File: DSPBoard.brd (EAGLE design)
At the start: 416 x 128.5 mm, 449 parts, among them IC1 AD1939WBSTZ, IC10 LM833D, IC11 LM833D, IC12 TL074D, IC2 24AA1025, IC29 TL074D, IC3 LM4040B10DBZ, IC4 LM833D, IC5 LM833D, IC6 LM833D, IC7 LM833D, IC8 LM833D, IC9 LM833D, U1 LM11173.3NOPB, U2 PEC11R-4315F-N0012, U3 PEC11R-4315F-N0012, X1 2510-, Y1 12.288MHz

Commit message: double-check and confirm opamp audio gains (not CV)
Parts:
- removed C133, C49, C58, C69: 10nF, rcl:C0603
- added C160: 10uF, rcl:C0603
- added C161: 0.1uF, rcl:C0603
- added CBST: 100nF, AcceleratedDesigns_Lib:0603
- added CIN: 22uF, AcceleratedDesigns_Lib:0805
- added COUT: 47uF, AcceleratedDesigns_Lib:1206
- added GND: WB_GND, AcceleratedDesigns_Lib:WB_GND
- added IOUT: WB_CURRENT_LOAD, AcceleratedDesigns_Lib:WB_CURRENT_LOAD
- added JP17, JP18, JP19, JP20: JUMPER-SMT_2_NC_PASTE_SILK, SparkFun-Jumpers:SMT-JUMPER_2_NC_PASTE_SILK
- added L1: 4.7uH, AcceleratedDesigns_Lib:CDPH4D19F
- added R182, R183, R184, R185: 100, rcl:R0603
- added RFBB: 10k, AcceleratedDesigns_Lib:0201
- added RFBT: 61.9k, AcceleratedDesigns_Lib:0402
- added SV2: (no value), con-lstb:MA04-1
- added U4: TPS561201DDCR, AcceleratedDesigns_Lib:DDC0006A
- added VIN: WB_BATTERY, AcceleratedDesigns_Lib:WB_BATTERY
- C119, C121: value 22uF -> 47uF; device rcl:C0603 -> rcl:PANASONIC_D
- C122: value 0.1u -> 390pF
- C123: value 0.1u -> 5.6nF
- C137: value 0.1uF -> 100uF
- C32: value 0.1uF -> 10uF
- R135: value 562 -> 562R
- R15, R31, R49, R65: value 15k -> 18k
- R364, R368, R369, R370: value 33R -> 2k2
- R39, R46, R62, R72: value 10k -> 6k2
- moved IC3 23.6 mm to (95.3, 32.7)
- moved C45 23.6 mm to (93.8, 34.0)
- moved J1 23.6 mm to (91.6, 31.4)
- moved R16 23.6 mm to (96.0, 31.4)
- moved R5 22.7 mm to (106.0, 14.5)
- moved R4 20.6 mm to (106.4, 12.6), turned to 180 degrees
- moved C29 19.9 mm to (108.6, 13.6), turned to 90 degrees
- moved U$11 17.6 mm to (112.4, 6.37), turned to 180 degrees
- moved C30 12.7 mm to (113.1, 17.5), turned to 270 degrees
- moved U$3 12.5 mm to (115.6, 17.0), flipped to the top, turned to 90 degrees
- moved C31 8.60 mm to (115.5, 14.0)
- moved SV1 7.73 mm to (123.6, 12.3), turned to 270 degrees
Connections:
- removed net DSDATA3: IC1.18
- removed net DSDATA4: IC1.15
- removed net N$234: D1.3, D3.3, D5.3, D7.3
- removed net N$235: D2.3, D4.3, D6.3, D8.3
- removed net N$549: IC2.6, R364.2
- removed net N$552: IC2.5, R368.2
- removed net N$553: R370.1, U$1.31
- removed net N$554: R369.1, U$1.30
- new net 0: CIN.2, COUT.2, GND.1, IOUT.2, RFBB.2, U4.1, VIN.2
- new net 1: CIN.1, U4.3, U4.5, VIN.1
- new net 2: CBST.1, L1.1, U4.2
- new net 3: RFBB.1, RFBT.2, U4.4
- new net 4: COUT.1, IOUT.1, L1.2, RFBT.1
- new net 5: CBST.2, U4.6
- new net N$135: IC1.35, JP20.1, SV2.1
- new net N$158: IC1.34, JP19.1, SV2.2
- new net N$159: IC1.31, JP18.1, SV2.3
- new net N$160: R182.2, R39.1
- new net N$161: R185.2, R46.1
- new net N$162: R183.2, R62.1
- new net N$163: R184.2, R72.1
- new net N$7: IC1.30, JP17.1, SV2.4
- net +3V3: now also C160.2, C161.2, R364.2, R368.1, R369.1, R370.1
- net AIN0+: now also D2.3
- net AIN0-: now also D1.3
- net AIN1+: now also D4.3
- net AIN1-: now also D3.3
- net AIN2+: now also D7.3
- net AIN2-: now also D8.3
- net AIN3+: now also D6.3
- net AIN3-: now also D5.3
- net ASDATA2: no longer IC1.26
- net DSDATA2: no longer IC1.19
- net FILTR: now also C121.+; no longer C121.1
- net GND: now also C119.-, C121.-, C160.1, C161.1, JP17.2, JP18.2, JP19.2, JP20.2; no longer C119.2, C121.2, IC1.30, IC1.31, IC1.34, IC1.35
- net MP2: now also IC2.6
- net MP3: now also IC2.5, R368.2; no longer R368.1
- net N$10: no longer C49.1
- net N$18: now also R182.1; no longer R39.1
- net N$36: now also R185.1; no longer R46.1
- net N$38: no longer C58.2
- net N$40: no longer C58.1
- net N$47: now also R183.1; no longer R62.1
- net N$48: no longer C69.2
- net N$49: no longer C69.1
- net N$56: now also R184.1; no longer R72.1
- net N$57: no longer C133.2
- net N$58: no longer C133.1
- net N$75: now also C119.+; no longer C119.1
- net N$9: no longer C49.2
- net S_SCL: now also U$1.31
- net S_SDA: now also U$1.30
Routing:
- net GND: track 153.9 -> 103.5 mm, vias 13 -> 16
- net +12V: track 50.8 -> 20.3 mm, vias 2 -> 1
- net +5V: track 41.3 -> 13.1 mm, vias 3 -> 1
- net N$8: track 4.24 -> 19.3 mm, vias 1 -> 0
- net -12V: track 5.11 -> 0.00 mm
- net N$5: track 13.7 -> 9.35 mm, vias 1 -> 2
- net N$2: track 4.12 -> 0.00 mm, vias 1 -> 0
- net N$554: track 2.60 -> 0.00 mm
- net N$553: track 2.57 -> 0.00 mm
- net DSDATA2: track 2.38 -> 0.01 mm
- added copper zone on layer 1, net +12V
- added copper zone on layer 1, net +5V
- added copper zone on layer 1, net GND
- added copper zone on layer 16, net GND
- added copper zone on layer 1, net N$2
- added copper zone on layer 1, net N$5
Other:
- outline, holes or cut-outs redrawn
- board text removed: "Power Supplies"

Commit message: Chekcing and some bug fixes complete, plus psu layout touchup
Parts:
- removed C156: 100n, rcl:C0603
- removed CBST: 100nF, AcceleratedDesigns_Lib:0603
- removed CIN: 22uF, AcceleratedDesigns_Lib:0805
- removed COUT: 47uF, AcceleratedDesigns_Lib:1206
- removed GND: WB_GND, AcceleratedDesigns_Lib:WB_GND
- removed IOUT: WB_CURRENT_LOAD, AcceleratedDesigns_Lib:WB_CURRENT_LOAD
- removed L1: 4.7uH, AcceleratedDesigns_Lib:CDPH4D19F
- removed MUX1_RIPPLECOUNTER, MUX2_RIPPLECOUNTER: 4024D, 40xx:SO14
- removed RFBB: 10k, AcceleratedDesigns_Lib:0201
- removed RFBT: 61.9k, AcceleratedDesigns_Lib:0402
- removed U4: TPS561201DDCR, AcceleratedDesigns_Lib:DDC0006A
- removed VIN: WB_BATTERY, AcceleratedDesigns_Lib:WB_BATTERY
- added IC13: 4520D, 45xx:SO16
- C128, C129, C130, C131, C146, C147, C150, C151: value 0.1u -> 1n
- moved U$29 242.3 mm to (234.9, -81.2)
- moved U$5 208.0 mm to (9.66, 120.7), turned to 0 degrees
- moved U$6 200.7 mm to (22.1, 120.7), turned to 0 degrees
- moved U$7 194.7 mm to (34.6, 120.7), turned to 0 degrees
- moved U$21 189.9 mm to (47.0, 120.7), turned to 0 degrees
- moved IC11 183.0 mm to (101.6, 103.2), turned to 180 degrees
- moved IC10 163.0 mm to (91.5, 103.2), turned to 180 degrees
- moved C124 156.0 mm to (9.73, -47.5), turned to 90 degrees
- moved R2 155.6 mm to (8.17, 89.8), turned to 0 degrees
- moved U$8 155.1 mm to (59.4, 120.7)
- moved C26 153.9 mm to (9.78, 79.1)
- moved U$10 152.8 mm to (7.03, 84.9), turned to 90 degrees
- moved C125 152.5 mm to (5.13, -44.0), turned to 90 degrees
- moved R3 151.2 mm to (11.2, 89.8), turned to 0 degrees
- moved R10 150.6 mm to (0.54, -40.3), turned to 0 degrees
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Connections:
- removed net 0: CIN.2, COUT.2, GND.1, IOUT.2, RFBB.2, U4.1, VIN.2
- removed net 1: CIN.1, U4.3, U4.5, VIN.1
- removed net 2: CBST.1, L1.1, U4.2
- removed net 3: RFBB.1, RFBT.2, U4.4
- removed net 4: COUT.1, IOUT.1, L1.2, RFBT.1
- removed net 5: CBST.2, U4.6
- net +5V: now also IC13.16; no longer C156.1, MUX1_RIPPLECOUNTER.14, MUX2_RIPPLECOUNTER.14
- net GND: now also IC12.12, IC12.5, IC13.8, IC29.12, IC29.5; no longer C156.2, IC12.13, IC12.6, IC29.13, IC29.6, MUX1_RIPPLECOUNTER.7, MUX2_RIPPLECOUNTER.7
- net MUX1_A: now also IC13.3; no longer MUX1_RIPPLECOUNTER.12
- net MUX1_B: now also IC13.4; no longer MUX1_RIPPLECOUNTER.11
- net MUX1_C: now also IC13.5; no longer MUX1_RIPPLECOUNTER.9
- net MUX2_A_A: now also IC13.11; no longer MUX2_RIPPLECOUNTER.12
- net MUX2_A_B: now also IC13.12; no longer MUX2_RIPPLECOUNTER.11
- net MUX2_A_C: now also IC13.13; no longer MUX2_RIPPLECOUNTER.9
- net N$116: now also IC12.6; no longer IC12.5
- net N$122: now also IC12.13; no longer IC12.12
- net N$540: now also IC29.6; no longer IC29.5
- net N$543: now also IC29.13; no longer IC29.12
- net SDATA_OUT2_LRCLK: now also IC13.1, IC13.9; no longer MUX1_RIPPLECOUNTER.1, MUX2_RIPPLECOUNTER.1
- net SEL1: now also IC13.10, IC13.2; no longer MUX1_RIPPLECOUNTER.2
- net SEL2: now also IC13.15, IC13.7; no longer MUX2_RIPPLECOUNTER.2
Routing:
- net +3V3: track 117.9 -> 17.0 mm, vias 10 -> 2
- net GND: track 103.5 -> 35.3 mm, vias 16 -> 9
- net N$212: track 52.7 -> 10.8 mm, vias 5 -> 0
- net N$31: track 38.6 -> 1.72 mm
- net N$32: track 45.6 -> 8.72 mm
- net 3V3A: track 18.7 -> 0.00 mm, vias 2 -> 0
- net N$6: track 4.16 -> 21.8 mm, vias 1 -> 0
- net +5V: track 13.1 -> 8.03 mm, vias 1 -> 0
- net N$27: track 3.34 -> 0.00 mm
- net N$28: track 3.94 -> 0.70 mm
- net S_AUX_ADC2: track 3.18 -> 0.00 mm
- net N$141: track 3.18 -> 0.00 mm
- net N$120: track 3.13 -> 0.00 mm
- net S_AUX_ADC1: track 3.02 -> 0.00 mm
- net RESET: track 2.90 -> 0.00 mm
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- added copper zone on layer 1, net 3V3A
- added copper zone on layer 1, net N$3
- added copper zone on layer 1, net N$4

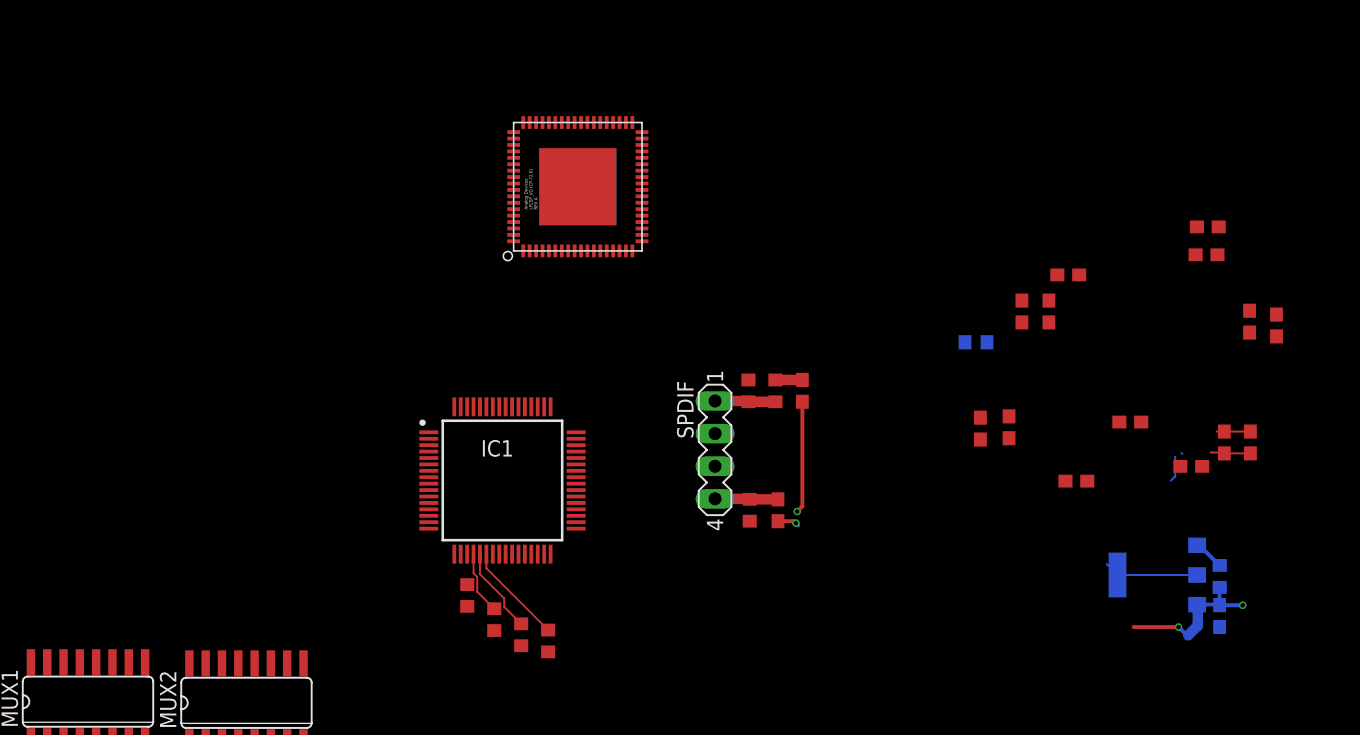
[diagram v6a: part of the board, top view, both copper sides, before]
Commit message: routing for the DSP
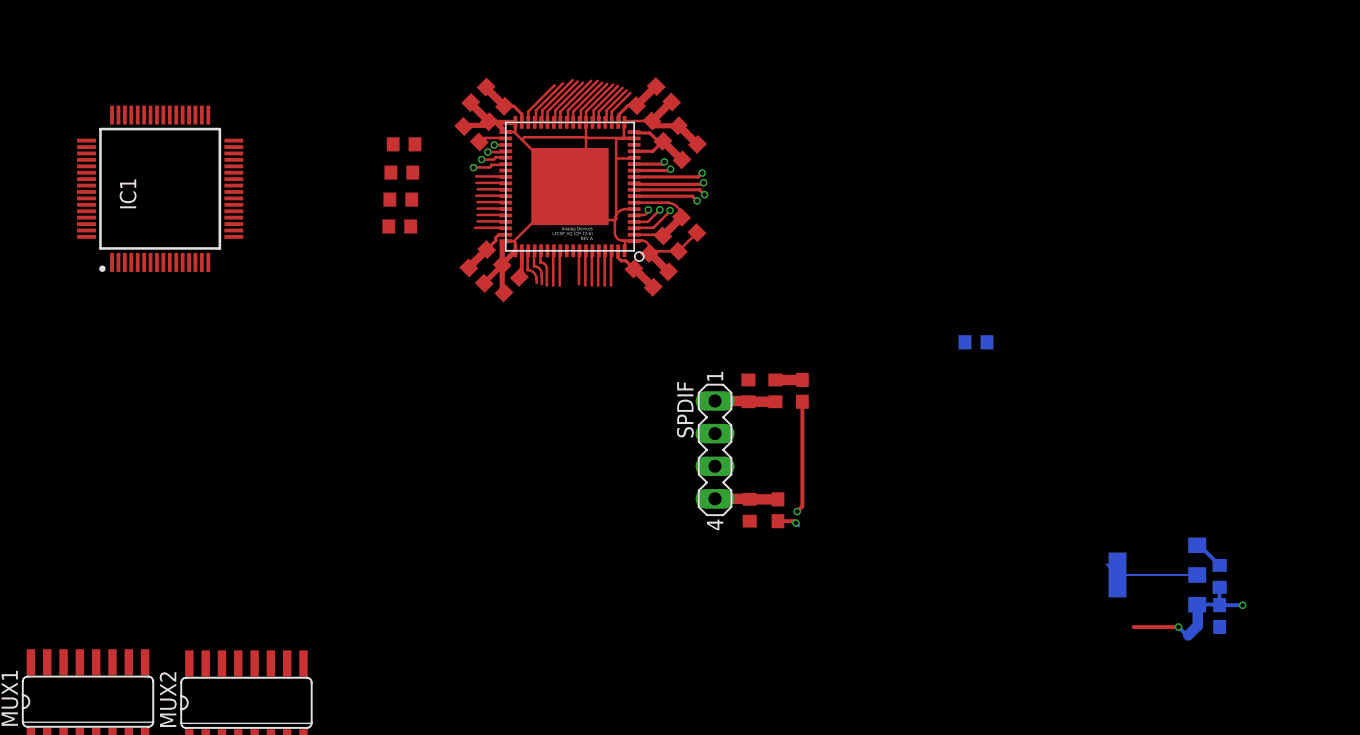
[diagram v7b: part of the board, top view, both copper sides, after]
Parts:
- moved C22 62.3 mm to (93.2, 83.9), turned to 135 degrees
- moved C15 60.6 mm to (95.0, 74.3), turned to 315 degrees
- moved C14 59.7 mm to (93.6, 72.9), turned to 315 degrees
- moved C16 47.7 mm to (110.2, 82.5), turned to 45 degrees
- moved C8 47.0 mm to (93.8, 87.0), turned to 225 degrees
- moved C7 46.8 mm to (95.2, 85.5), turned to 225 degrees
- moved C19 46.6 mm to (96.4, 72.1), turned to 225 degrees
- moved C13 44.0 mm to (106.5, 74.0), turned to 45 degrees
- moved C18 43.4 mm to (110.2, 76.8), turned to 315 degrees
- moved C11 42.8 mm to (108.0, 72.6), turned to 45 degrees
- moved R18 40.3 mm to (88.0, 83.1), turned to 0 degrees
- moved C21 38.4 mm to (108.7, 75.4), turned to 315 degrees
- moved R19 37.2 mm to (87.8, 80.9), turned to 0 degrees
- moved C9 35.1 mm to (106.7, 85.5), turned to 315 degrees
- moved IC1 35.0 mm to (69.0, 79.6), turned to 90 degrees
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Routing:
- net GND: track 35.3 -> 120.6 mm
- net +3V3: track 17.0 -> 36.3 mm
- net N$212: track 10.8 -> 24.5 mm
- net DLRCLK: track 7.90 -> 0.00 mm
- net DBCLK: track 6.76 -> 0.00 mm
- net S_AUX_ADC1: track 0.00 -> 5.64 mm, vias 0 -> 1
- net S_AUX_ADC2: track 0.00 -> 5.49 mm, vias 0 -> 1
- net S_AUX_ADC3: track 0.00 -> 5.43 mm, vias 0 -> 1
- net S_AUX_ADC0: track 0.00 -> 5.05 mm, vias 0 -> 1
- net DSDATA1: track 4.92 -> 0.01 mm
- net N$157: track 0.00 -> 4.30 mm
- net MP2: track 0.00 -> 4.23 mm
- net MP3: track 0.00 -> 4.23 mm
- net S_SCL: track 0.00 -> 4.16 mm
- net MP1: track 0.00 -> 4.02 mm
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
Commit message: grinding through
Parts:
- moved IC13 691.6 mm to (355.1, 142.4)
- moved JP10 582.5 mm to (368.5, 31.3)
- moved JP9 563.6 mm to (359.2, 16.6), turned to 270 degrees
- moved C160 562.1 mm to (218.3, 148.0)
- moved C161 562.1 mm to (218.3, 143.1)
- moved JP14 562.1 mm to (249.4, 174.7)
- moved JP15 562.1 mm to (240.8, 174.7)
- moved JP16 562.1 mm to (232.2, 174.7)
- moved R182 533.5 mm to (196.4, 118.1)
- moved R184 527.4 mm to (176.2, 133.1)
- moved C159 520.5 mm to (218.8, 83.7), flipped to the bottom, turned to 90 degrees
- moved JP2 519.0 mm to (390.5, 16.3)
- moved R183 516.1 mm to (167.2, 131.0)
- moved JP20 492.8 mm to (182.5, 75.3)
- moved JP19 489.0 mm to (180.0, 75.3)
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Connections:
- net ASDATA2: now also IC1.26
- net DSDATA2: now also IC1.19
- net ENCODER0_0: now also JP4.2; no longer JP4.1
- net S_AUX_ADC1: now also JP4.1; no longer JP4.2
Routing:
- net RESET: track 3.67 -> 108.1 mm, vias 0 -> 2
- net GND: track 120.6 -> 216.7 mm, vias 9 -> 10
- net +3V3: track 36.3 -> 124.0 mm, vias 2 -> 3
- net 1452_CLK_OUT: track 0.00 -> 53.9 mm, vias 0 -> 1
- net S_SCL: track 4.16 -> 56.0 mm
- net S_SDA: track 4.02 -> 50.6 mm
- net ABCLK: track 0.00 -> 39.4 mm, vias 0 -> 1
- net ALRCLK: track 0.00 -> 38.1 mm, vias 0 -> 1
- net ASDATA1: track 0.00 -> 36.2 mm, vias 0 -> 1
- net ASDATA2: track 0.00 -> 35.3 mm, vias 0 -> 1
- net MP2: track 4.23 -> 33.6 mm, vias 0 -> 2
- net N$134: track 2.42 -> 30.2 mm
- net MP3: track 4.23 -> 31.1 mm, vias 0 -> 2
- net N$132: track 2.22 -> 28.3 mm
- net S_AUX_ADC0: track 5.05 -> 31.1 mm
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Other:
- board text added: "I2c Address"
- board text added: "SelfBoot"
